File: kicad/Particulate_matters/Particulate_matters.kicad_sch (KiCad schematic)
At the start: 4 parts, among them U1 XIAO-ESP32-S3-DIP

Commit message: updated pcb
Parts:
- added U5: ~, Connector_PinSocket_2.54mm:PinSocket_1x04_P2.54mm_Vertical, symbol ParticulateMatters:SSD1306_128x32_0.91
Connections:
- net GND: now also U5.1 (GND)
- net VCC: now also U5.2 (VCC)
- net at U1.5 (GPIO5/D4/I2C_SDA), U3.3 (SDA): now also U5.4 (SDA)
- net at U1.6 (GPIO9/D5/I2C_SCL), U3.4 (SDL): now also U5.3 (SCK)
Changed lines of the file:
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@@
 	(generator_version "9.0")
 	(paper "A4")
+	(junction
+		(at 104.14 99.06)
+		(diameter 0)
+		(color 0 0 0 0)
+	)
+	(junction
+		(at 101.6 95.25)
+		(diameter 0)
+		(color 0 0 0 0)
+	)
 	(wire
 		(pts
@@
 	(wire
 		(pts
+			(xy 161.29 111.76) (xy 101.6 111.76)
+		)
+		(stroke
+			(width 0)
+			(type default)
+		)
+	)
+	(wire
+		(pts
 			(xy 161.29 76.2) (xy 194.31 76.2)
 		)
@@
 	(wire
 		(pts
+			(xy 153.67 100.33) (xy 161.29 100.33)
+		)
+		(stroke
+			(width 0)
+			(type default)
+		)
+	)
+	(wire
+		(pts
+			(xy 153.67 104.14) (xy 161.29 104.14)
+		)
+		(stroke
+			(width 0)
+			(type default)
+		)
+	)
+	(wire
+		(pts
 			(xy 161.29 68.58) (xy 175.26 68.58)
 		)
@@
 	(wire
 		(pts
+			(xy 101.6 111.76) (xy 101.6 95.25)
+		)
+		(stroke
+			(width 0)
+			(type default)
+		)
+	)
+	(wire
+		(pts
 			(xy 170.18 83.82) (xy 170.18 80.01)
 		)
@@
 	(wire
 		(pts
+			(xy 161.29 107.95) (xy 104.14 107.95)
+		)
+		(stroke
+			(width 0)
+			(type default)
+		)
+	)
+	(wire
+		(pts
 			(xy 161.29 72.39) (xy 194.31 72.39)
 		)
@@
 	(wire
 		(pts
+			(xy 104.14 107.95) (xy 104.14 99.06)
+		)
+		(stroke
+			(width 0)
+			(type default)
+		)
+	)
+	(wire
+		(pts
 			(xy 175.26 68.58) (xy 175.26 80.01)
 		)
@@
 	(hierarchical_label "GND"
 		(shape input)
+		(at 153.67 100.33 180)
+		(effects
+			(font
+				(size 1.27 1.27)
+			)
+			(justify right)
+		)
+	)
+	(hierarchical_label "GND"
+		(shape input)
 		(at 74.93 60.96 0)
 		(effects
@@
 			)
 			(justify left)
+		)
+	)
+	(hierarchical_label "VCC"
+		(shape input)
+		(at 153.67 104.14 180)
+		(effects
+			(font
+				(size 1.27 1.27)
+			)
+			(justify right)
 		)
 	)
@@
 					(unit 1)
 				)
+			)
+		)
+	)
+	(symbol
+		(lib_id "ParticulateMatters:SSD1306_128x32_0.91")
+		(at 226.06 96.52 0)
+		(mirror y)
+		(unit 1)
+		(exclude_from_sim no)
+		(in_bom yes)
+		(on_board yes)
+		(dnp no)
+		(fields_autoplaced yes)
+		(property "Reference" "U5"
+			(at 227.33 104.7721 0)
+			(effects
+				(font
+					(size 1.27 1.27)
+				)
+				(justify right)
+			)
+		)
+		(property "Value" "~"
+			(at 227.33 106.6772 0)
+			(effects
+				(font
+					(size 1.27 1.27)
+				)
+				(justify right)
+			)
+		)
+		(property "Footprint" "Connector_PinSocket_2.54mm:PinSocket_1x04_P2.54mm_Vertical"
+			(at 226.06 96.52 0)
+			(effects
+				(font
+					(size 1.27 1.27)
+				)
+				(hide yes)
+			)
+		)
+		(property "Datasheet" ""
+			(at 226.06 96.52 0)
+			(effects
+				(font
+					(size 1.27 1.27)
+				)
+				(hide yes)
+			)
+		)
+		(property "Description" ""
+			(at 226.06 96.52 0)
+			(effects
+				(font
+					(size 1.27 1.27)
+				)
+				(hide yes)
+			)
+		)
+		(pin "2"
+		)
+		(pin "1"
+		)
+		(pin "3"
+		)
+		(pin "4"
+		)
+		(instances
+			(project ""
+				(path "/a469de4a-6558-4c6c-9733-dd68d37b40f4"
+					(reference "U5")
+					(unit 1)
+				)

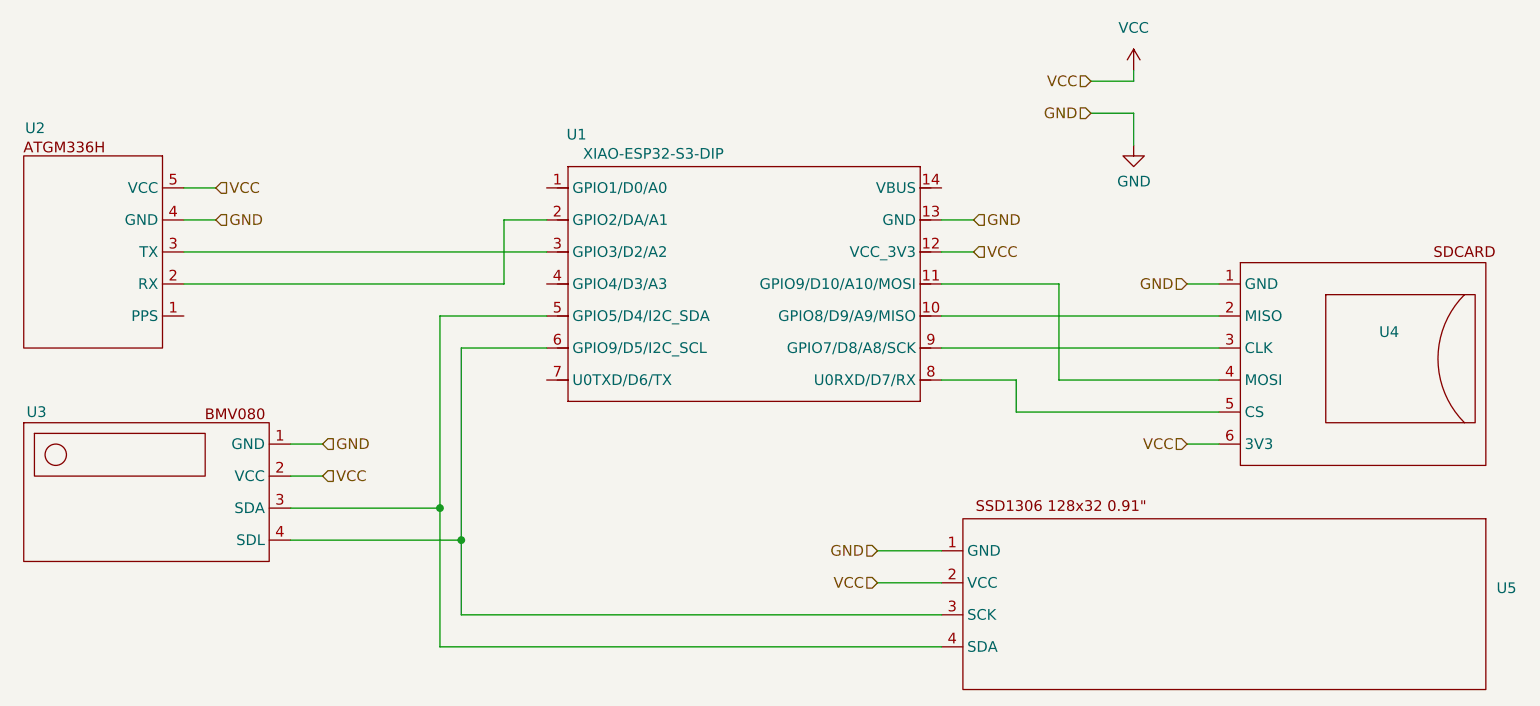
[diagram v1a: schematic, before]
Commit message: AI updated version in _fixed.ino, readme now uses the svg diagram
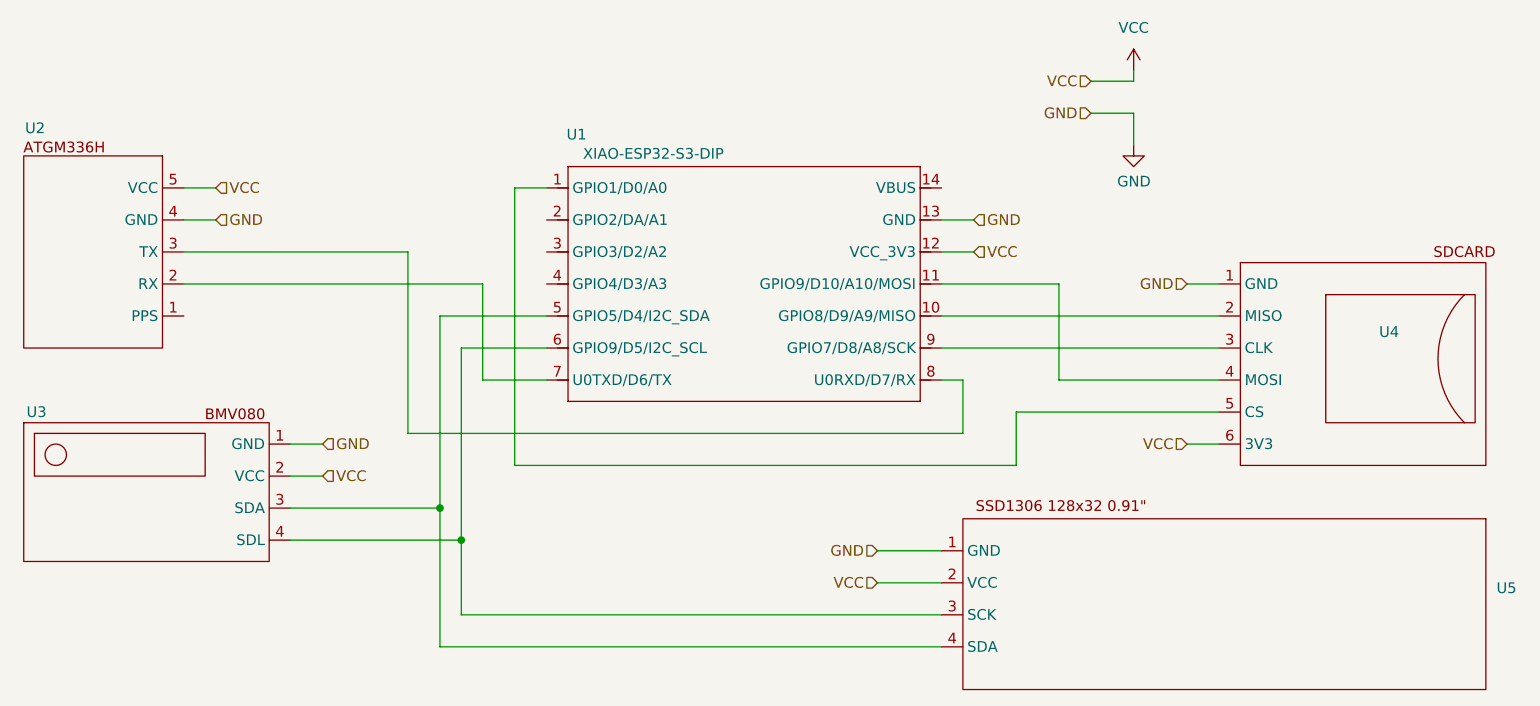
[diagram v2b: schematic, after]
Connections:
- net at U1.1 (GPIO1/D0/A0): now also U4.5 (CS)
- net at U1.2 (GPIO2/DA/A1): no longer U2.2 (RX)
- net at U1.3 (GPIO3/D2/A2): no longer U2.3 (TX)
- net at U1.7 (U0TXD/D6/TX): now also U2.2 (RX)
- net at U1.8 (U0RXD/D7/RX): now also U2.3 (TX); no longer U4.5 (CS)
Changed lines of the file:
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@@
+	(wire
+		(pts
+			(xy 71.12 64.77) (xy 97.79 64.77)
+		)
+		(stroke
+			(width 0)
+			(type default)
+		)
+	)
 	(wire
 		(pts
@@
 	(wire
 		(pts
+			(xy 106.68 68.58) (xy 106.68 80.01)
+		)
+		(stroke
+			(width 0)
+			(type default)
+		)
+	)
+	(wire
+		(pts
 			(xy 71.12 60.96) (xy 74.93 60.96)
 		)
@@
 	(wire
 		(pts
+			(xy 110.49 90.17) (xy 170.18 90.17)
+		)
+		(stroke
+			(width 0)
+			(type default)
+		)
+	)
+	(wire
+		(pts
 			(xy 71.12 57.15) (xy 74.93 57.15)
 		)
@@
 	(wire
 		(pts
-			(xy 71.12 64.77) (xy 114.3 64.77)
+			(xy 97.79 86.36) (xy 163.83 86.36)
 		)
 		(stroke
@@
 	(wire
 		(pts
+			(xy 97.79 64.77) (xy 97.79 86.36)
+		)
+		(stroke
+			(width 0)
+			(type default)
+		)
+	)
+	(wire
+		(pts
 			(xy 104.14 76.2) (xy 114.3 76.2)
 		)
@@
 	(wire
 		(pts
+			(xy 163.83 86.36) (xy 163.83 80.01)
+		)
+		(stroke
+			(width 0)
+			(type default)
+		)
+	)
+	(wire
+		(pts
+			(xy 163.83 80.01) (xy 161.29 80.01)
+		)
+		(stroke
+			(width 0)
+			(type default)
+		)
+	)
+	(wire
+		(pts
 			(xy 190.5 87.63) (xy 194.31 87.63)
 		)
@@
 	(wire
 		(pts
-			(xy 170.18 83.82) (xy 170.18 80.01)
-		)
-		(stroke
-			(width 0)
-			(type default)
-		)
-	)
-	(wire
-		(pts
 			(xy 190.5 68.58) (xy 194.31 68.58)
 		)
@@
 	(wire
 		(pts
+			(xy 170.18 90.17) (xy 170.18 83.82)
+		)
+		(stroke
+			(width 0)
+			(type default)
+		)
+	)
+	(wire
+		(pts
 			(xy 175.26 80.01) (xy 194.31 80.01)
 		)
@@
 	(wire
 		(pts
-			(xy 170.18 80.01) (xy 161.29 80.01)
-		)
-		(stroke
-			(width 0)
-			(type default)
-		)
-	)
-	(wire
-		(pts
-			(xy 109.22 68.58) (xy 109.22 60.96)
-		)
-		(stroke
-			(width 0)
-			(type default)
-		)
-	)
-	(wire
-		(pts
-			(xy 109.22 60.96) (xy 114.3 60.96)
+			(xy 114.3 57.15) (xy 110.49 57.15)
+		)
+		(stroke
+			(width 0)
+			(type default)
+		)
+	)
+	(wire
+		(pts
+			(xy 110.49 57.15) (xy 110.49 90.17)
 		)
 		(stroke
@@
 	(wire
 		(pts
+			(xy 106.68 80.01) (xy 114.3 80.01)
+		)
+		(stroke
+			(width 0)
+			(type default)
+		)
+	)
+	(wire
+		(pts
 			(xy 184.15 48.26) (xy 184.15 52.07)
 		)
@@
 	(wire
 		(pts
-			(xy 71.12 68.58) (xy 109.22 68.58)
-		)
-		(stroke
+			(xy 71.12 68.58) (xy 106.68 68.58)
+		)
+		(stroke
